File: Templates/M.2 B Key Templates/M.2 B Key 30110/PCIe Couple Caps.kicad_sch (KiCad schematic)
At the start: 2 parts

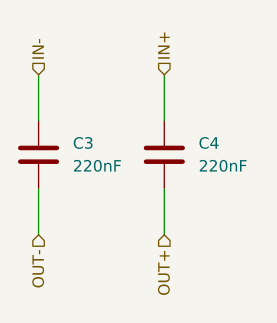
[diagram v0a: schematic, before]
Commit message: Added B Key Templates
-added B key Templates for all sizes
-corrected B key symbol pinout
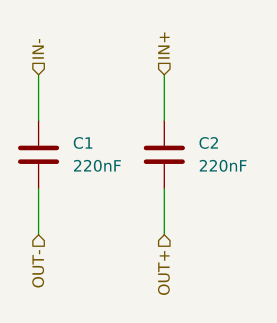
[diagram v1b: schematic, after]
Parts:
- renumbered C3 to C1, C4 to C2
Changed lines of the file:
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@@
 		(dnp no)
 		(fields_autoplaced yes)
-		(property "Reference" "C?"
+		(property "Reference" "C1"
 			(at 133.35 99.0599 0)
 			(effects
@@
 		)
 		(instances
-			(project "M.2 A Key 2230"
-				(path "/540e8a72-89ee-4807-aaa2-5d6c6cec308d/6a934661-433b-4364-b7d9-86a36dc44459/424c4cf5-3c3c-49ef-81c3-66eb0f823d39"
+			(project "M.2 B key 30110"
+				(path "/214bfc41-24f4-4af9-b8d5-f53b552105c4/a97a1c5a-89b8-4965-a918-3f182150b9ea/27d77bf0-8499-4672-87f1-05095c3d0a68"
 					(reference "C3")
 					(unit 1)
 				)
-				(path "/540e8a72-89ee-4807-aaa2-5d6c6cec308d/6a934661-433b-4364-b7d9-86a36dc44459/adcd4998-a306-4f2e-b87b-352712eb899b"
-					(reference "C2")
-					(unit 1)
-				)
-			)
-			(project "M.2 A Key"
-				(path "/d21209cf-d1f8-4eb7-aed8-e43843eefa7b/424c4cf5-3c3c-49ef-81c3-66eb0f823d39"
-					(reference "C?")
-					(unit 1)
-				)
-				(path "/d21209cf-d1f8-4eb7-aed8-e43843eefa7b/adcd4998-a306-4f2e-b87b-352712eb899b"
-					(reference "C?")
+				(path "/214bfc41-24f4-4af9-b8d5-f53b552105c4/a97a1c5a-89b8-4965-a918-3f182150b9ea/2cd6dc77-f114-44b1-9704-d60d213c1d42"
+					(reference "C1")
 					(unit 1)
 				)
@@
 		(dnp no)
 		(fields_autoplaced yes)
-		(property "Reference" "C?"
+		(property "Reference" "C2"
 			(at 147.32 99.0599 0)
 			(effects
@@
 		)
 		(instances
-			(project "M.2 A Key 2230"
-				(path "/540e8a72-89ee-4807-aaa2-5d6c6cec308d/6a934661-433b-4364-b7d9-86a36dc44459/424c4cf5-3c3c-49ef-81c3-66eb0f823d39"
+			(project "M.2 B key 30110"
+				(path "/214bfc41-24f4-4af9-b8d5-f53b552105c4/a97a1c5a-89b8-4965-a918-3f182150b9ea/27d77bf0-8499-4672-87f1-05095c3d0a68"
 					(reference "C4")
 					(unit 1)
 				)
-				(path "/540e8a72-89ee-4807-aaa2-5d6c6cec308d/6a934661-433b-4364-b7d9-86a36dc44459/adcd4998-a306-4f2e-b87b-352712eb899b"
-					(reference "C1")
+				(path "/214bfc41-24f4-4af9-b8d5-f53b552105c4/a97a1c5a-89b8-4965-a918-3f182150b9ea/2cd6dc77-f114-44b1-9704-d60d213c1d42"
+					(reference "C2")
 					(unit 1)
 				)
-			)
-			(project "M.2 A Key"
-				(path "/d21209cf-d1f8-4eb7-aed8-e43843eefa7b/424c4cf5-3c3c-49ef-81c3-66eb0f823d39"
-					(reference "C?")
-					(unit 1)
-				)
-				(path "/d21209cf-d1f8-4eb7-aed8-e43843eefa7b/adcd4998-a306-4f2e-b87b-352712eb899b"
-					(reference "C?")
-					(unit 1)
-				)
